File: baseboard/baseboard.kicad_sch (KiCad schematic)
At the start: 41 parts, among them J1 SWD, J2 USB_C_Receptacle_USB2.0_16P, J3 DISP, SW1 SW_Push, SW2 RST, U1 nRF52833-QDxx, U2 MCP1700x-330xxMB, X2 32kHz, Y1 32MHz

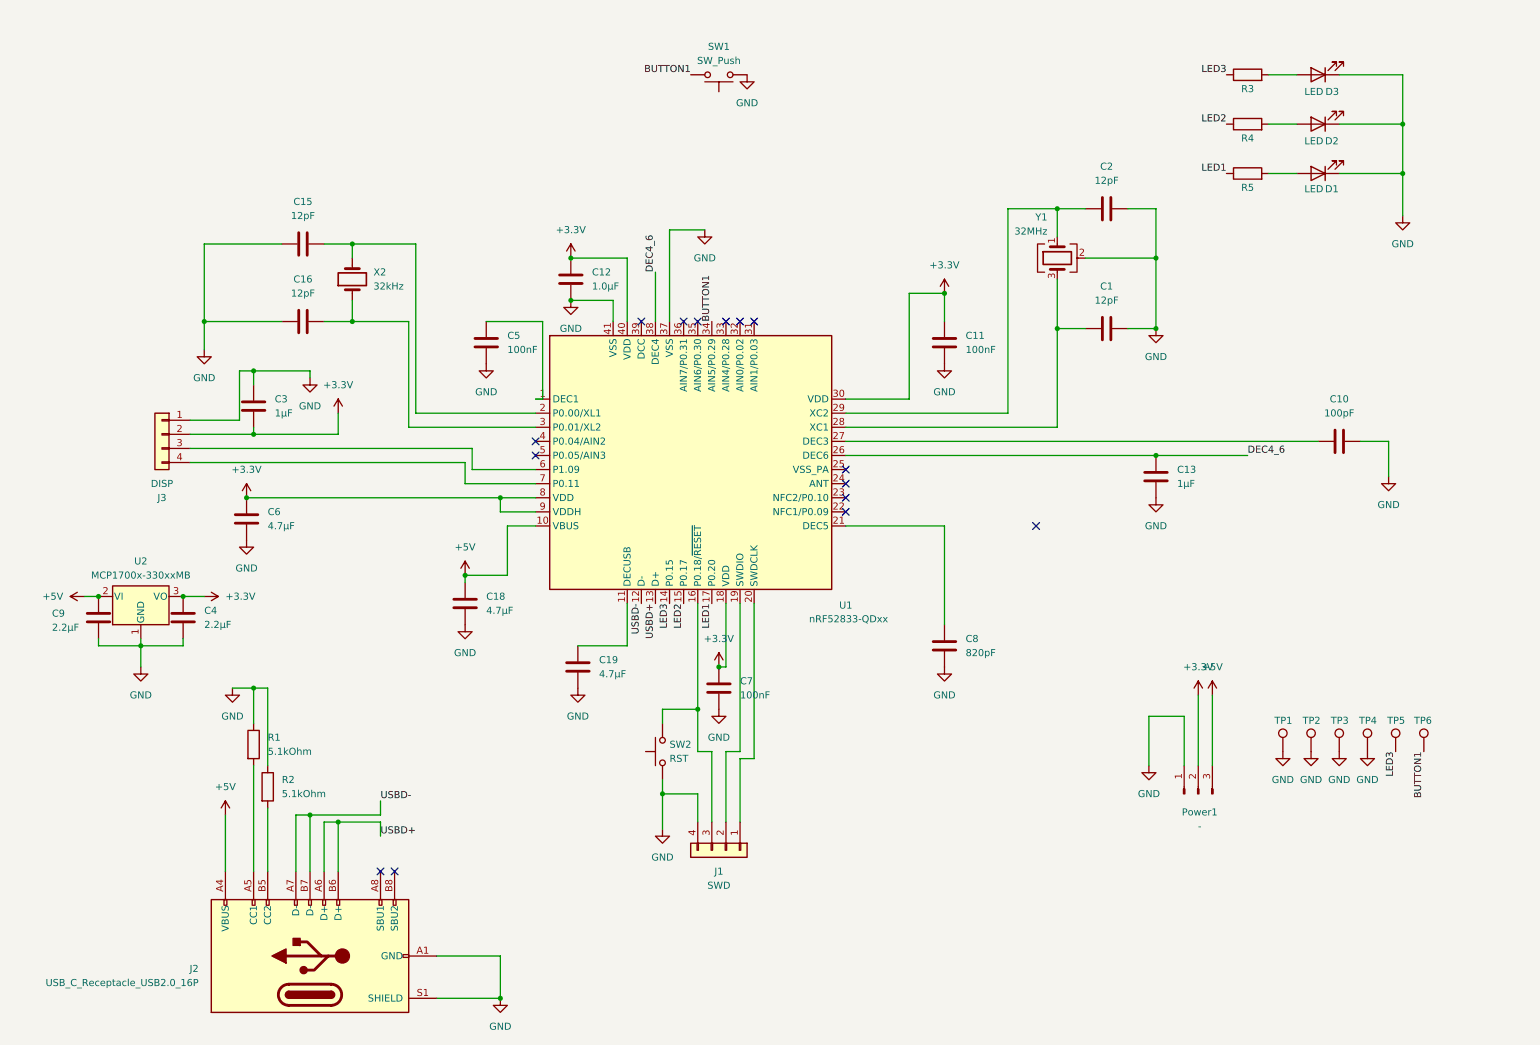
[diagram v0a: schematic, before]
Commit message: Finished schematic & pcb design with extra components
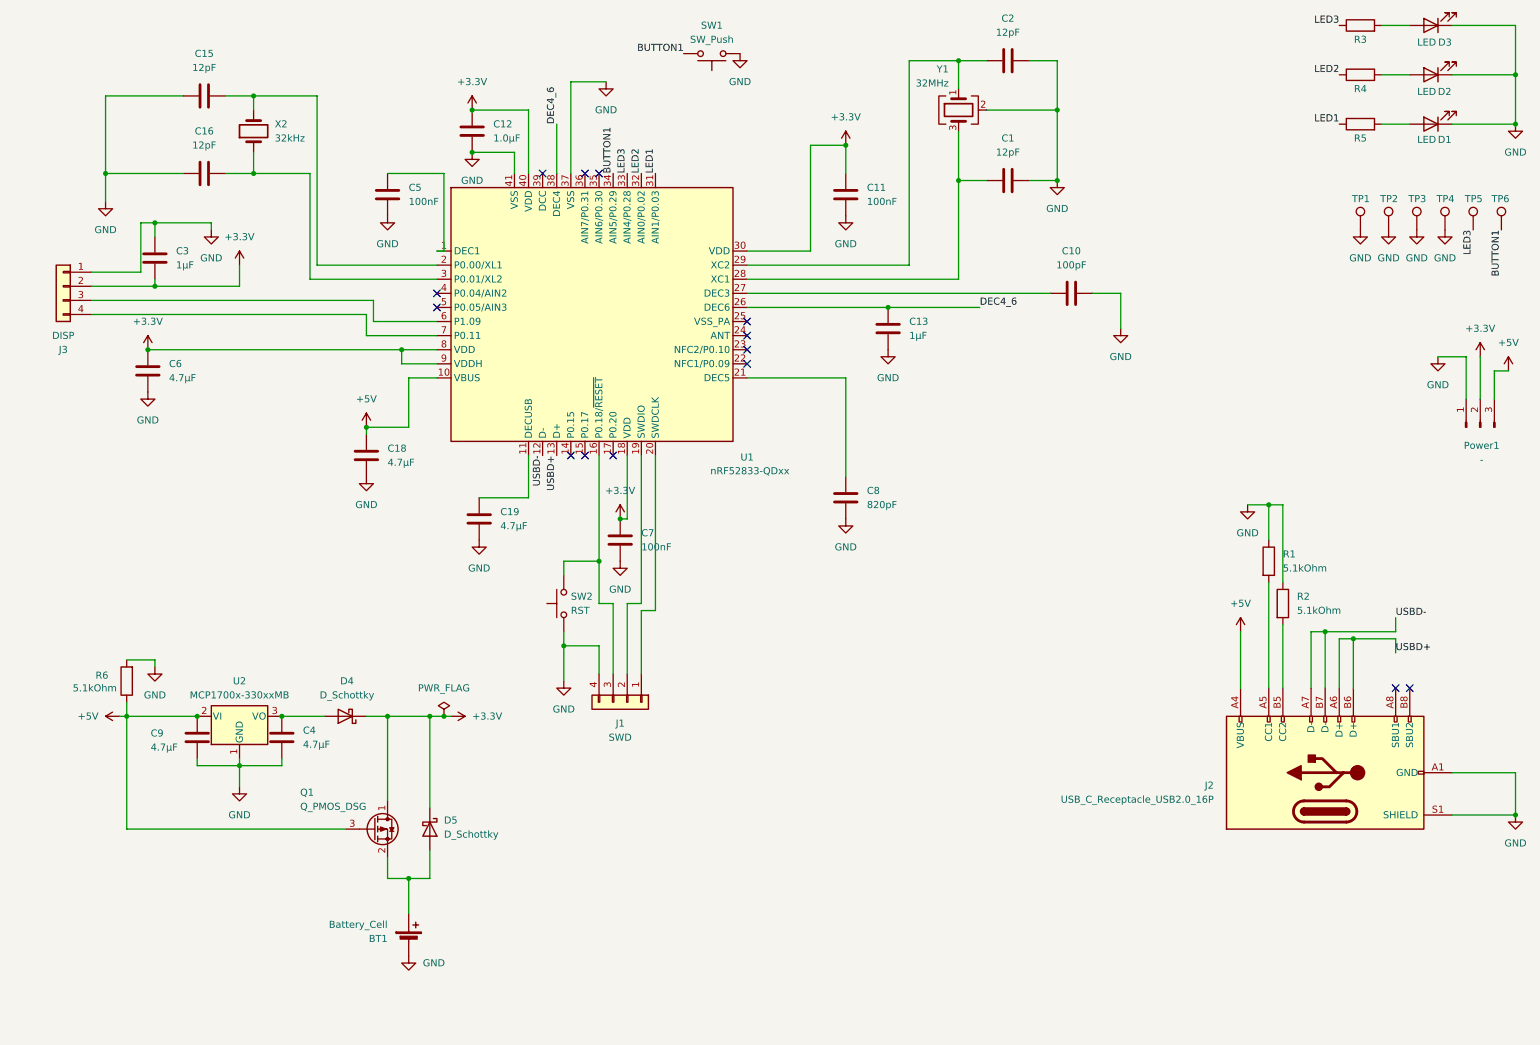
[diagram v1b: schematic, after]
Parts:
- added BT1: Battery_Cell, Battery:BatteryHolder_Keystone_3002_1x2032, symbol Device:Battery_Cell
- added D4, D5: D_Schottky, Diode_SMD:D_SOD-123, symbol Device:D_Schottky
- added Q1: Q_PMOS_DSG, Package_TO_SOT_SMD:SOT-23, symbol Transistor_FET:Q_PMOS_DSG
- added R6: 5.1kOhm, Resistor_SMD:R_0603_1608Metric, symbol Device:R
- C4, C9: value 2.2µF -> 4.7µF
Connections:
- net +3.3V: now also D4.1 (K), D5.1 (K), Q1.1 (D); no longer C4.1, U2.3 (VO)
- net +5V: now also Q1.3 (G), R6.1
- net GND: now also BT1.2 (-), R6.2
- net LED1: now also U1.31 (AIN1/P0.03); no longer U1.17 (P0.20)
- net LED2: now also U1.32 (AIN0/P0.02); no longer U1.15 (P0.17)
- net LED3: now also U1.33 (AIN4/P0.28); no longer U1.14 (P0.15)
- new net: C4.1, D4.2 (A), U2.3 (VO)
- new net: BT1.1 (+), D5.2 (A), Q1.2 (S)
- no-connect marks 15 -> 14
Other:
- moved on the sheet: C1, C10, C11, C12, C13, C15, C16, C18, C19, C2, C3, C4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

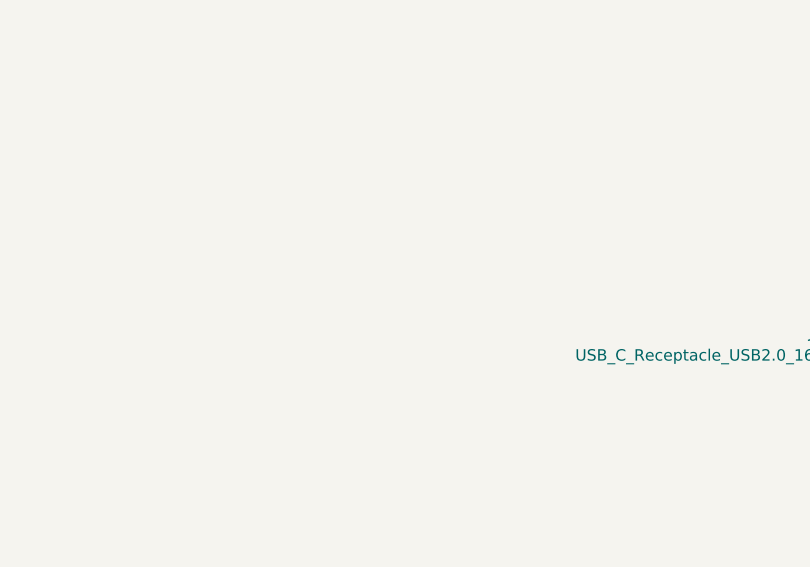
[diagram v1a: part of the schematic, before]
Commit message: Fixed PCB and added an extra USB-A connector
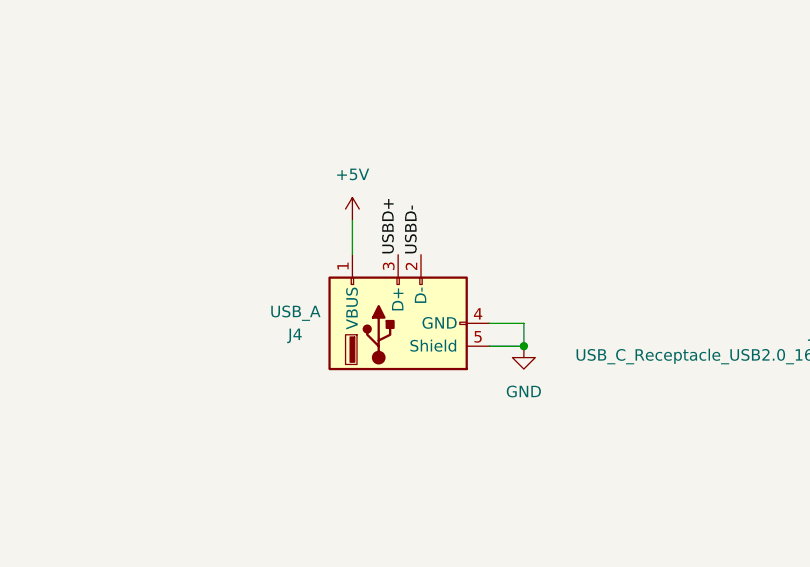
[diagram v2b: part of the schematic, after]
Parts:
- added J4: USB_A, Connector_USB:USB_A_Molex_48037-2200_Horizontal, symbol Connector:USB_A
- SW1, SW2: footprint Button_Switch_THT:SW_PUSH_6mm_H9.5mm -> Button_Switch_THT:SW_PUSH_6mm
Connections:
- net +5V: now also J4.1 (VBUS)
- net GND: now also J4.4 (GND), J4.5 (Shield)
- net USBD+: now also J4.3 (D+)
- net USBD-: now also J4.2 (D-)
